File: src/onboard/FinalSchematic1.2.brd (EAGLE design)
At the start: 137.6 x 80 mm, 84 parts, among them IC1 MIC29310-5.0BT, IC3 A5975D

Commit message: Added new BMP280 component to onboard
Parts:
- removed BMP280_I2C: (no value), con-lstb:MA07-1
- added U1: ADAFRUIT_BMP280_BAROMETER, AERO_Eagle_Library:ADAFRUIT_BMP280_BAROMETER
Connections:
- removed net 3V0: BMP280_I2C.2
- new net 3VO: U1.3VO
- net CS: now also U1.CS; no longer BMP280_I2C.7
- net GND: now also U1.GND; no longer BMP280_I2C.3
- net SCK: now also U1.SCK; no longer BMP280_I2C.4
- net SDI: now also U1.SDI; no longer BMP280_I2C.6
- net SDO: now also U1.SDO; no longer BMP280_I2C.5
- net VIN: now also U1.VIN; no longer BMP280_I2C.1
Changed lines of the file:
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@@
 <attribute name="VALUE" x="-34.671" y="-123.952" size="1.27" layer="27" ratio="10"/>
 </element>
-<element name="BMP280_I2C" library="con-lstb" library_urn="urn:adsk.eagle:library:162" package="MA07-1" package3d_urn="urn:adsk.eagle:package:8341/1" value="" x="-25.908" y="-128.016" smashed="yes">
-<attribute name="MF" value="" x="-25.908" y="-128.016" size="1.778" layer="27" display="off"/>
-<attribute name="MPN" value="" x="-25.908" y="-128.016" size="1.778" layer="27" display="off"/>
-<attribute name="NAME" x="-34.798" y="-126.365" size="1.27" layer="25" ratio="10"/>
-<attribute name="OC_FARNELL" value="unknown" x="-25.908" y="-128.016" size="1.778" layer="27" display="off"/>
-<attribute name="OC_NEWARK" value="unknown" x="-25.908" y="-128.016" size="1.778" layer="27" display="off"/>
-<attribute name="POPULARITY" value="4" x="-25.908" y="-128.016" size="1.778" layer="27" display="off"/>
-<attribute name="VALUE" x="-28.448" y="-130.937" size="1.27" layer="27" ratio="10"/>
-</element>
+<element name="U1" library="AERO_Eagle_Library" package="ADAFRUIT_BMP280_BAROMETER" value="ADAFRUIT_BMP280_BAROMETER" x="-35.56" y="-149.352" smashed="yes"/>
 </elements>
 <signals>
@@
 <contactref element="AUX" pad="1"/>
 <contactref element="C2" pad="2"/>
-<contactref element="BMP280_I2C" pad="3"/>
-<wire x1="-31.75" y1="-120.904" x2="-28.448" y2="-128.016" width="0" layer="19" extent="1-1"/>
+<contactref element="U1" pad="GND"/>
+<wire x1="-31.75" y1="-120.904" x2="-29.21" y2="-146.812" width="0" layer="19" extent="1-1"/>
 <wire x1="-33.528" y1="-115.316" x2="-31.75" y2="-120.904" width="0" layer="19" extent="1-1"/>
 <wire x1="-34.798" y1="-110.236" x2="-33.528" y2="-115.316" width="0" layer="19" extent="1-1"/>
@@
 </signal>
 <signal name="VIN">
-<contactref element="BMP280_I2C" pad="1"/>
-</signal>
-<signal name="3V0">
-<contactref element="BMP280_I2C" pad="2"/>
+<contactref element="U1" pad="VIN"/>
 </signal>
 <signal name="SCK">
-<contactref element="BMP280_I2C" pad="4"/>
+<contactref element="U1" pad="SCK"/>
 </signal>
 <signal name="SDO">
-<contactref element="BMP280_I2C" pad="5"/>
+<contactref element="U1" pad="SDO"/>
 </signal>
 <signal name="SDI">
-<contactref element="BMP280_I2C" pad="6"/>
+<contactref element="U1" pad="SDI"/>
 </signal>
 <signal name="CS">
-<contactref element="BMP280_I2C" pad="7"/>
+<contactref element="U1" pad="CS"/>
+</signal>
+<signal name="3VO">
+<contactref element="U1" pad="3VO"/>
 </signal>
 </signals>

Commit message: First routing attempt Still need to fix silkscreen
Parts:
- removed SV16: (no value), con-lstb:MA03-1
- removed TP1, TP2, TP3, TP4, TP5: PTR1B1,27, testpad:B1,27
- added 22V, 5V, 6V, SCL, SDA: PTR1B1,27, testpad:B1,27
- added C4: 10uF, capacitor-wima:C2.5-3
- added SV0: (no value), con-lstb:MA03-1
- moved AUX 227.1 mm to (95.0, 73.7), turned to 180 degrees
- moved R23 222.4 mm to (89.4, 76.7), turned to 180 degrees
- moved U1 218.0 mm to (68.6, 42.2), turned to 90 degrees
- moved C2 215.4 mm to (64.5, 71.1), turned to 90 degrees
- moved C1 176.3 mm to (37.6, 57.9), turned to 270 degrees
- moved 5V_PWR 176.0 mm to (36.6, 73.2), turned to 270 degrees
- moved U$2 170.8 mm to (127.0, 72.9)
- moved IC1 170.4 mm to (45.2, 61.5), turned to 270 degrees
- moved 22V_PWR 156.7 mm to (48.3, 73.7), turned to 270 degrees
- moved 6V_PWR 143.8 mm to (42.7, 73.2), turned to 270 degrees
- moved BTNBANK 111.3 mm to (71.6, 4.06), turned to 180 degrees
- moved R22 110.8 mm to (74.3, 11.7), turned to 270 degrees
- moved U$4 110.7 mm to (7.62, 7.62)
- moved RADIO 109.1 mm to (127.5, 65.5), turned to 270 degrees
- moved R19 105.6 mm to (70.1, 11.7), turned to 270 degrees
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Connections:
- removed net 22_INPUT: R1.2
- removed net 3VO: U1.3VO
- removed net CS: U1.CS
- removed net SCK: U1.SCK
- removed net SDI: U1.SDI
- removed net SDO: U1.SDO
- removed net VIN: U1.VIN
- net 22V_INPUT: now also 22V.TP, R1.2; no longer TP4.TP
- net 5V: now also 5V.TP, SV0.2, U1.VIN; no longer SV16.2, TP1.TP
- net 6V: now also 6V.TP, C4.1; no longer TP5.TP
- net BTN1: no longer TEENSY4.1.24-A10/TX6/SCL2
- net BTN2: no longer TEENSY4.1.25-A11/RX6/SDA2
- net GND: now also C4.2, SV0.3; no longer SV16.3
- net N$100: now also SV0.1; no longer SV14.1
- net N$105: now also SV4.1; no longer SV11.1
- net N$108: now also SV5.1; no longer SV10.1
- net N$109: now also SV9.1; no longer SV5.1
- net N$112: now also SV15.1; no longer SV9.1
- net N$115: now also SV14.1; no longer SV6.1
- net N$118: now also SV13.1; no longer SV4.1
- net N$2: now also SV12.1; no longer SV3.1
- net N$43: now also SV11.1; no longer SV16.1
- net N$81: now also SV7.1; no longer SV13.1
- net N$82: now also SV3.1; no longer SV15.1
- net N$85: now also SV2.1; no longer SV8.1
- net N$88: now also SV6.1; no longer SV7.1
- net N$91: now also SV10.1; no longer SV2.1
- net N$94: now also SV8.1; no longer SV1.1
- net N$97: now also SV1.1; no longer SV12.1
- net O_LED: now also TEENSY4.1.41-A17/MISO1; no longer TEENSY4.1.40-A16/CS1
- net PWM0: now also R5.1; no longer R4.1
- net PWM1: now also R2.1; no longer R3.1
- net PWM11: now also R10.1; no longer R12.1
- net PWM14: now also R17.1; no longer R16.1
- net PWM15: now also R16.1; no longer R17.1
- net PWM2: now also R3.1; no longer R2.1
- net PWM3: now also R4.1; no longer R15.1
- net PWM4: now also R9.1; no longer R5.1
- net PWM5: now also R8.1; no longer R6.1
- net PWM7: now also R6.1; no longer R8.1
- net PWM8: now also R15.1; no longer R9.1
- net PWM9: now also R12.1; no longer R10.1
- net R_LED: now also TEENSY4.1.38-A14/CS/IN1; no longer TEENSY4.1.41-A17/MISO1
- net SCL: now also SCL.TP, U1.SCK; no longer TP3.TP
- net SDA: now also SDA.TP, U1.SDI; no longer TP2.TP
- net SELECT_PIN: now also TEENSY4.1.31-CTX3; no longer TEENSY4.1.2-OUT2
- net W_LED: now also TEENSY4.1.40-A16/CS1; no longer TEENSY4.1.38-A14/CS/IN1
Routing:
- net 5V: track 83.8 -> 522.9 mm
- net GND: track 366.9 -> 0.25 mm, vias 8 -> 142
- net B_LED: track 4.86 -> 58.9 mm
- net DIP1: track 42.9 -> 95.1 mm, vias 1 -> 0
- net DIP2: track 43.9 -> 89.6 mm, vias 1 -> 0
- net 22V_INPUT: track 10.0 -> 51.7 mm
- net DIP3: track 42.9 -> 83.8 mm, vias 1 -> 0
- net BTN1: track 0.00 -> 39.7 mm
- net R_LED: track 15.2 -> 53.8 mm
- net BTN2: track 0.00 -> 34.8 mm
- net SDA: track 109.1 -> 142.6 mm
- net Y_LED: track 16.1 -> 48.7 mm
- net DIP4: track 46.0 -> 78.3 mm, vias 1 -> 0
- net SCK0: track 0.00 -> 31.7 mm
- net W_LED: track 14.3 -> 43.6 mm
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- added copper zone on layer 16, net GND
- removed copper zone on layer 16, net 5V
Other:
- board size 137.6 x 80 mm -> 134.6 x 80.5 mm
- board text added: "ONLY CONNECT ONE SUPPLY!"
- board text added: "V1.3"
- board text added: "Western Aero Design 2022"
- board text removed: "5V"
- board text removed: "Blue"
- board text removed: "DIP1"
- board text removed: "DIP2"
- board text removed: "DIP3"
- board text removed: "DIP4"
- board text removed: "GND"
- board text removed: "Green"
- board text removed: "Orange"
- board text removed: "PT Sig"
- board text removed: "Pwr"
- board text removed: "Red"
- board text removed: "SCL"
- board text removed: "SDA"
- board text removed: "Signal"
- board text removed: "Slct Pin"
- board text removed: "White"
- board text removed: "Yllw"
- board text removed: "pin10"
- board text removed: "pin11"
- board text removed: "pin12"
- board text removed: "pin13"
- board text removed: "pin16"
- board text removed: "pin17"
- board text removed: "pin24"
- board text removed: "pin25"
- board text removed: "pin29"
- board text removed: "pin31"
- board text removed: "pin5"
- board text removed: "pin6"

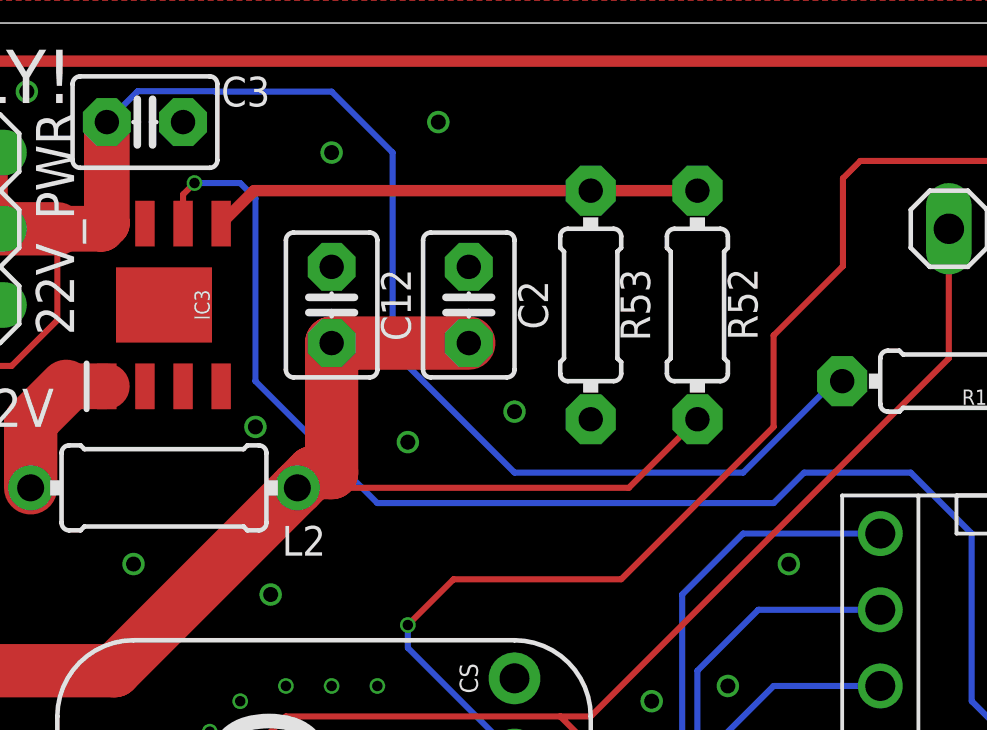
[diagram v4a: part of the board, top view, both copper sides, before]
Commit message: Added 3.3 solderpad
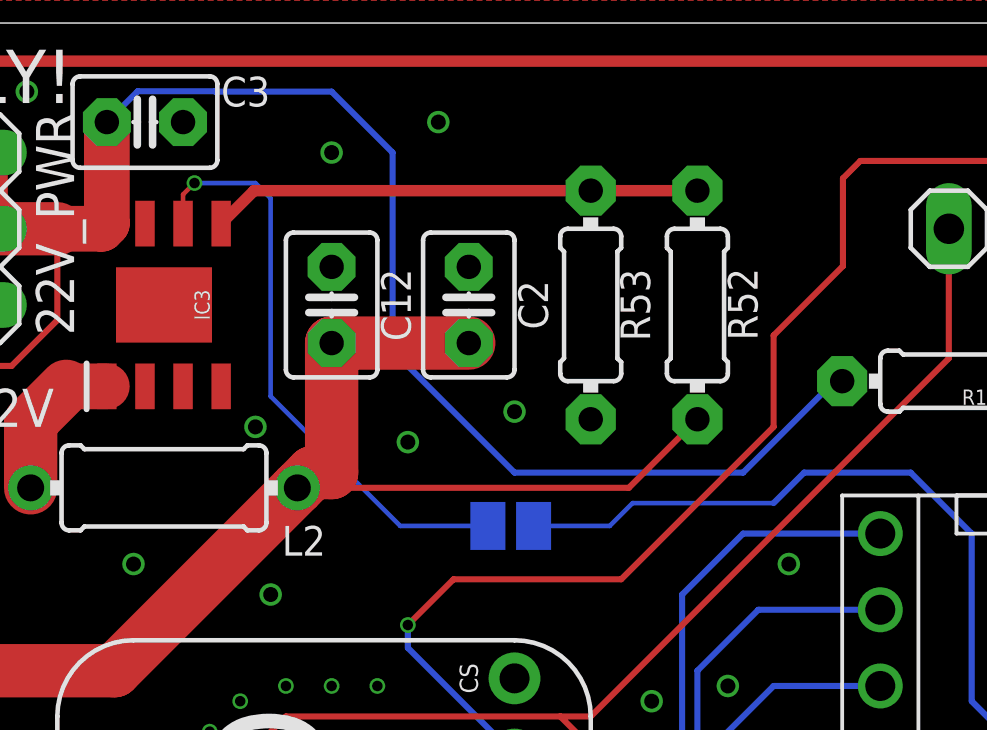
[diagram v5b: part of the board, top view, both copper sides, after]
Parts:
- added SJ1: (no value), jumper:SJ
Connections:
- new net N$3: IC3.6, SJ1.1
- net 3.3V: now also SJ1.2; no longer IC3.6
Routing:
- net 3.3V: track 106.6 -> 86.1 mm, vias 1 -> 0
- net N$3: track 0.00 -> 19.9 mm, vias 0 -> 1
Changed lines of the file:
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@@
 <attribute name="VALUE" x="34.544" y="65.151" size="1.27" layer="27" ratio="10" rot="R270"/>
+</element>
+<element name="SJ1" library="jumper" library_urn="urn:adsk.eagle:library:252" package="SJ" package3d_urn="urn:adsk.eagle:package:15471/1" value="" x="65.913" y="63.754" smashed="yes" rot="MR180">
+<attribute name="NAME" x="64.262" y="62.611" size="1.27" layer="26" ratio="10" rot="MR180"/>
+<attribute name="POPULARITY" value="33" x="65.913" y="63.754" size="1.778" layer="28" rot="MR180" display="off"/>
+<attribute name="VALUE" x="66.3131" y="63.754" size="0.02" layer="28" rot="MR180"/>
 </element>
 </elements>
@@
 </signal>
 <signal name="3.3V">
-<contactref element="IC3" pad="6"/>
 <contactref element="TEENSY4.1" pad="3V3-3"/>
 <contactref element="TEENSY4.1" pad="3V3-2"/>
@@
 <wire x1="81.28" y1="63.5" x2="79.248" y2="65.532" width="0.2032" layer="16"/>
 <wire x1="79.248" y1="65.532" x2="75.692" y2="65.532" width="0.2032" layer="16"/>
-<wire x1="75.692" y1="65.532" x2="74.676" y2="64.516" width="0.2032" layer="16"/>
-<wire x1="74.676" y1="64.516" x2="61.468" y2="64.516" width="0.2032" layer="16"/>
-<wire x1="61.468" y1="64.516" x2="57.404" y2="68.58" width="0.2032" layer="16"/>
-<wire x1="57.404" y1="74.676" x2="56.896" y2="75.184" width="0.2032" layer="16"/>
-<wire x1="56.896" y1="75.184" x2="55.372" y2="75.184" width="0.2032" layer="16"/>
-<via x="55.372" y="75.184" extent="1-16" drill="0.35"/>
-<wire x1="55.372" y1="75.184" x2="54.991" y2="74.803" width="0.2032" layer="1"/>
-<wire x1="54.991" y1="74.803" x2="54.991" y2="73.832" width="0.2032" layer="1"/>
-<wire x1="57.404" y1="68.58" x2="57.404" y2="74.676" width="0.2032" layer="16"/>
+<wire x1="74.676" y1="64.516" x2="75.692" y2="65.532" width="0.2032" layer="16"/>
+<contactref element="SJ1" pad="2"/>
+<wire x1="66.675" y1="63.754" x2="69.215" y2="63.754" width="0.1524" layer="16"/>
+<wire x1="69.977" y1="64.516" x2="69.215" y2="63.754" width="0.1524" layer="16"/>
+<wire x1="69.977" y1="64.516" x2="74.676" y2="64.516" width="0.1524" layer="16"/>
 </signal>
 <signal name="PWM0">
@@
 <wire x1="90.424" y1="53.848" x2="93.472" y2="50.8" width="0.2032" layer="1"/>
 </signal>
+<signal name="N$3">
+<contactref element="IC3" pad="6"/>
+<contactref element="SJ1" pad="1"/>
+<wire x1="54.991" y1="73.832" x2="54.991" y2="74.803" width="0.1524" layer="1"/>
+<wire x1="54.991" y1="74.803" x2="55.372" y2="75.184" width="0.1524" layer="1"/>
+<via x="55.372" y="75.184" extent="1-16" drill="0.35"/>
+<wire x1="55.372" y1="75.184" x2="57.404" y2="75.184" width="0.1524" layer="16"/>
+<wire x1="57.404" y1="75.184" x2="57.912" y2="74.676" width="0.1524" layer="16"/>
+<wire x1="57.912" y1="74.676" x2="57.912" y2="68.072" width="0.1524" layer="16"/>
+<wire x1="62.23" y1="63.754" x2="65.151" y2="63.754" width="0.1524" layer="16"/>
+<wire x1="57.912" y1="68.072" x2="62.23" y2="63.754" width="0.1524" layer="16"/>
+</signal>
 </signals>
